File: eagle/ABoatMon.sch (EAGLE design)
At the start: 26 parts, among them J1 5V, J2 GND, J3 GND, J4 5V

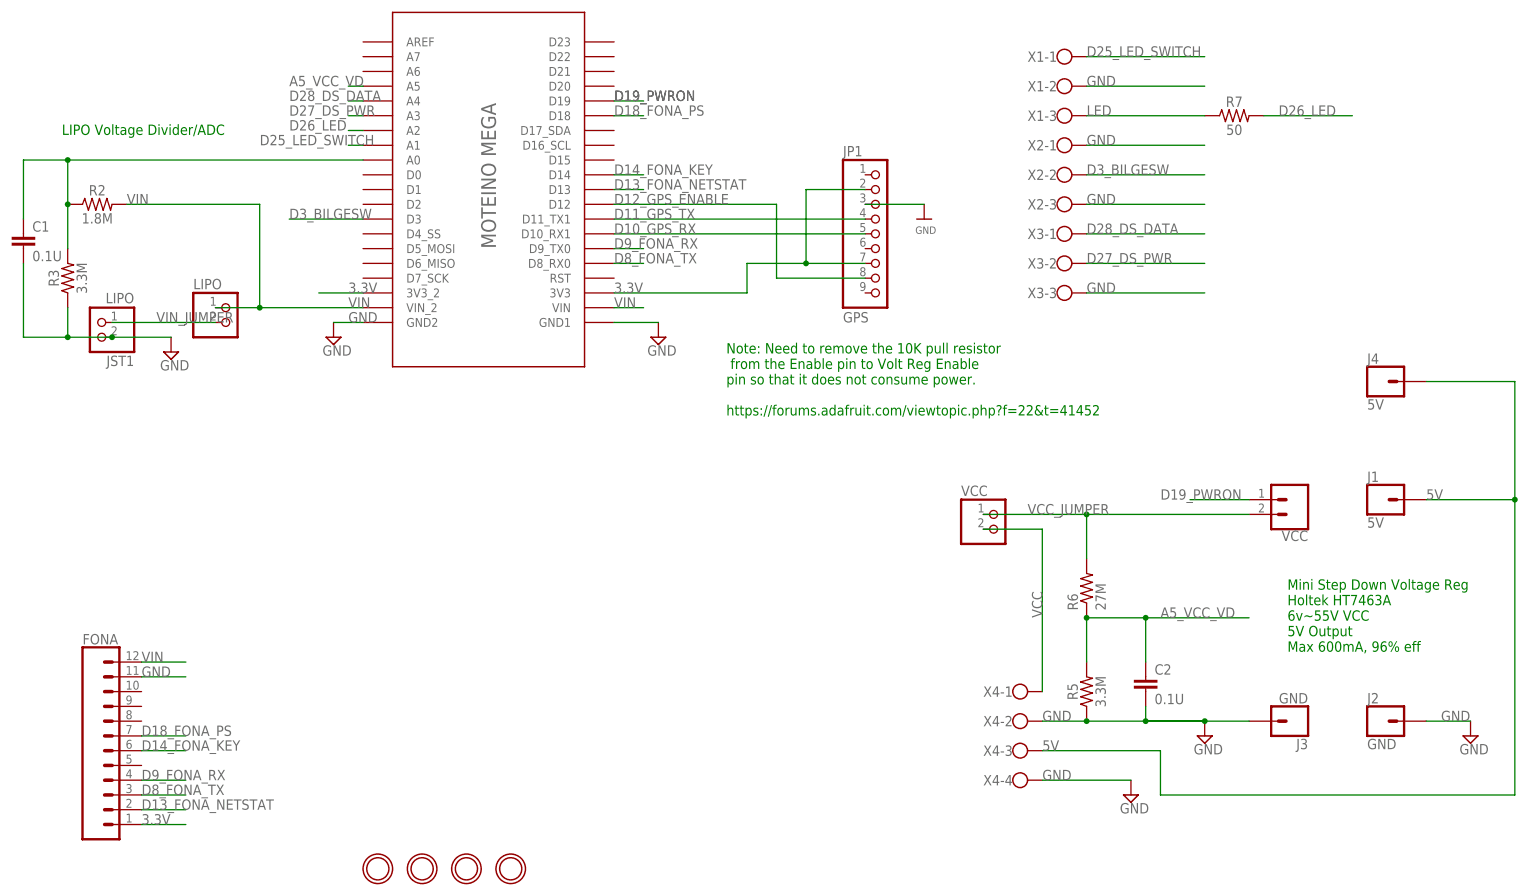
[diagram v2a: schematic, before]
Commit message: v0.649 - rotate gps, fona, move TH parts, remove 5v and GND screw
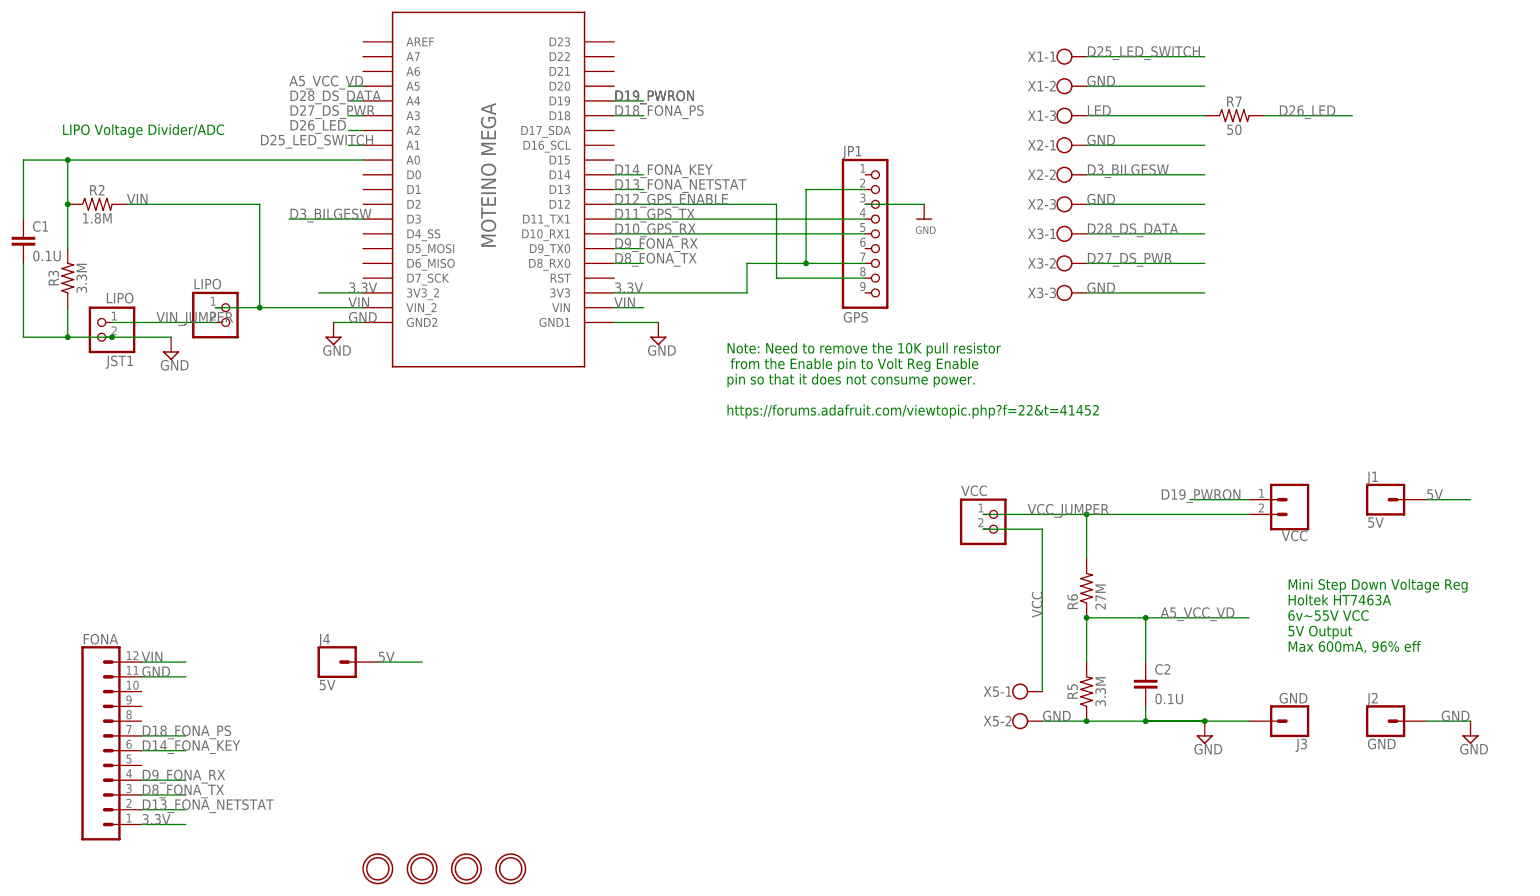
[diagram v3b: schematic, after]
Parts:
- removed X4: (no value), con-wago-500:W237-4
- added X5: (no value), con-wago-500:W237-102
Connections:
- net 5V: no longer X4-3.KL
- net GND: now also X5-2.KL; no longer X4-2.KL, X4-4.KL
- net VCC: now also X5-1.KL; no longer X4-1.KL
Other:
- moved on the sheet: J4
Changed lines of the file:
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@@
 <attributes>
 <attribute name="CNAME" value="MoteinoMega ABoatMon Shield"/>
-<attribute name="CREVISION" value="0.549"/>
+<attribute name="CREVISION" value="0.649"/>
 <attribute name="DESIGNER" value="gregcope@gmail.com"/>
 </attributes>
@@
 <part name="ENABLE" library="SparkFun-Connectors" deviceset="CONN_02" device="" value="VCC"/>
 <part name="SUPPLY9" library="supply2" deviceset="GND" device=""/>
-<part name="SUPPLY10" library="supply2" deviceset="GND" device=""/>
 <part name="R6" library="adafruit" deviceset="R-US_" device="0309/12" value="27M"/>
 <part name="FONA" library="SparkFun-Connectors" deviceset="CONN_12" device=""/>
@@
 <part name="X2" library="con-wago-500" library_urn="urn:adsk.eagle:library:195" deviceset="W237-103" device="" package3d_urn="urn:adsk.eagle:package:10691/1"/>
 <part name="X3" library="con-wago-500" library_urn="urn:adsk.eagle:library:195" deviceset="W237-103" device="" package3d_urn="urn:adsk.eagle:package:10691/1"/>
-<part name="X4" library="con-wago-500" library_urn="urn:adsk.eagle:library:195" deviceset="W237-4" device="" package3d_urn="urn:adsk.eagle:package:10695/1"/>
 <part name="U$2" library="microbuilder" deviceset="MOUNTINGHOLE" device="2.5"/>
 <part name="U$3" library="microbuilder" deviceset="MOUNTINGHOLE" device="2.5"/>
@@
 <part name="LIPO" library="microbuilder" deviceset="HEADER-1X2" device="ROUND"/>
 <part name="J4" library="SparkFun-Connectors" deviceset="CONN_01" device="" value="5V"/>
+<part name="X5" library="con-wago-500" library_urn="urn:adsk.eagle:library:195" deviceset="W237-102" device="" package3d_urn="urn:adsk.eagle:package:10688/1"/>
 </parts>
 <sheets>
@@
 <attribute name="VALUE" x="252.095" y="40.005" size="1.778" layer="96"/>
 </instance>
-<instance part="SUPPLY10" gate="GND" x="195.58" y="33.02" smashed="yes">
-<attribute name="VALUE" x="193.675" y="29.845" size="1.778" layer="96"/>
-</instance>
 <instance part="R6" gate="G$1" x="187.96" y="68.58" smashed="yes" rot="R90">
 <attribute name="NAME" x="186.4614" y="64.77" size="1.778" layer="95" rot="R90"/>
@@
 <attribute name="VALUE" x="180.34" y="115.697" size="1.778" layer="96"/>
 <attribute name="NAME" x="182.88" y="120.269" size="1.778" layer="95" rot="R180"/>
-</instance>
-<instance part="X4" gate="-1" x="175.26" y="50.8" smashed="yes">
-<attribute name="NAME" x="175.26" y="51.689" size="1.778" layer="95" rot="R180"/>
-</instance>
-<instance part="X4" gate="-2" x="175.26" y="45.72" smashed="yes">
-<attribute name="NAME" x="175.26" y="46.609" size="1.778" layer="95" rot="R180"/>
-</instance>
-<instance part="X4" gate="-3" x="175.26" y="40.64" smashed="yes">
-<attribute name="NAME" x="175.26" y="41.529" size="1.778" layer="95" rot="R180"/>
-</instance>
-<instance part="X4" gate="-4" x="175.26" y="35.56" smashed="yes">
-<attribute name="VALUE" x="172.72" y="31.877" size="1.778" layer="96"/>
-<attribute name="NAME" x="175.26" y="36.449" size="1.778" layer="95" rot="R180"/>
 </instance>
 <instance part="U$2" gate="G$1" x="66.04" y="20.32" smashed="yes"/>
@@
 <attribute name="VALUE" x="34.29" y="109.22" size="1.778" layer="96"/>
 </instance>
-<instance part="J4" gate="G$1" x="238.76" y="104.14" smashed="yes">
-<attribute name="VALUE" x="236.22" y="99.314" size="1.778" layer="96" font="vector"/>
-<attribute name="NAME" x="236.22" y="107.188" size="1.778" layer="95" font="vector"/>
+<instance part="J4" gate="G$1" x="58.42" y="55.88" smashed="yes">
+<attribute name="VALUE" x="55.88" y="51.054" size="1.778" layer="96" font="vector"/>
+<attribute name="NAME" x="55.88" y="58.928" size="1.778" layer="95" font="vector"/>
+</instance>
+<instance part="X5" gate="-1" x="175.26" y="50.8" smashed="yes">
+<attribute name="NAME" x="175.26" y="51.689" size="1.778" layer="95" rot="R180"/>
+</instance>
+<instance part="X5" gate="-2" x="175.26" y="45.72" smashed="yes">
+<attribute name="VALUE" x="172.72" y="42.037" size="1.778" layer="96"/>
+<attribute name="NAME" x="175.26" y="46.609" size="1.778" layer="95" rot="R180"/>
 </instance>
 </instances>
@@
 <junction x="198.12" y="45.72"/>
 <pinref part="J3" gate="G$1" pin="1"/>
-<pinref part="X4" gate="-2" pin="KL"/>
+<pinref part="X5" gate="-2" pin="KL"/>
 </segment>
 <segment>
@@
 <label x="60.96" y="114.3" size="1.778" layer="95"/>
 <pinref part="SUPPLY3" gate="GND" pin="GND"/>
-</segment>
-<segment>
-<pinref part="SUPPLY10" gate="GND" pin="GND"/>
-<pinref part="X4" gate="-4" pin="KL"/>
-<wire x1="195.58" y1="35.56" x2="180.34" y2="35.56" width="0.1524" layer="91"/>
-<label x="180.34" y="35.56" size="1.778" layer="95"/>
 </segment>
 </net>
@@
 <segment>
 <label x="180.34" y="63.5" size="1.778" layer="95" rot="R90"/>
-<pinref part="X4" gate="-1" pin="KL"/>
 <wire x1="180.34" y1="78.74" x2="180.34" y2="50.8" width="0.1524" layer="91"/>
 <pinref part="VCC" gate="G$1" pin="2"/>
 <wire x1="170.18" y1="78.74" x2="180.34" y2="78.74" width="0.1524" layer="91"/>
+<pinref part="X5" gate="-1" pin="KL"/>
 </segment>
 </net>
@@
 <segment>
 <label x="246.38" y="83.82" size="1.778" layer="95"/>
-<wire x1="246.38" y1="83.82" x2="261.62" y2="83.82" width="0.1524" layer="91"/>
-<wire x1="261.62" y1="83.82" x2="261.62" y2="33.02" width="0.1524" layer="91"/>
-<wire x1="261.62" y1="33.02" x2="200.66" y2="33.02" width="0.1524" layer="91"/>
-<wire x1="200.66" y1="33.02" x2="200.66" y2="40.64" width="0.1524" layer="91"/>
-<wire x1="200.66" y1="40.64" x2="180.34" y2="40.64" width="0.1524" layer="91"/>
-<label x="180.34" y="40.64" size="1.778" layer="95"/>
+<wire x1="246.38" y1="83.82" x2="254" y2="83.82" width="0.1524" layer="91"/>
 <pinref part="J1" gate="G$1" pin="1"/>
-<pinref part="X4" gate="-3" pin="KL"/>
+</segment>
+<segment>
 <pinref part="J4" gate="G$1" pin="1"/>
-<wire x1="246.38" y1="104.14" x2="261.62" y2="104.14" width="0.1524" layer="91"/>
-<wire x1="261.62" y1="104.14" x2="261.62" y2="83.82" width="0.1524" layer="91"/>
-<junction x="261.62" y="83.82"/>
-</segment>
-</net>
+<wire x1="66.04" y1="55.88" x2="73.66" y2="55.88" width="0.1524" layer="91"/>
+<label x="66.04" y="55.88" size="1.778" layer="95"/>
+</segment>
+</net>
